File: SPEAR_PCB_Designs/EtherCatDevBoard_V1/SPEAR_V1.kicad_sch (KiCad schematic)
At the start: 25 parts, among them J1 Conn_ARM_SWD_TagConnect_TC2030, J2 USB_C_Receptacle_USB2.0_16P, SW1 SW_Push, SW2 SW_Push, U1 STM32F446RCTx, U2 USBLC6-2SC6, Y1 16MHz

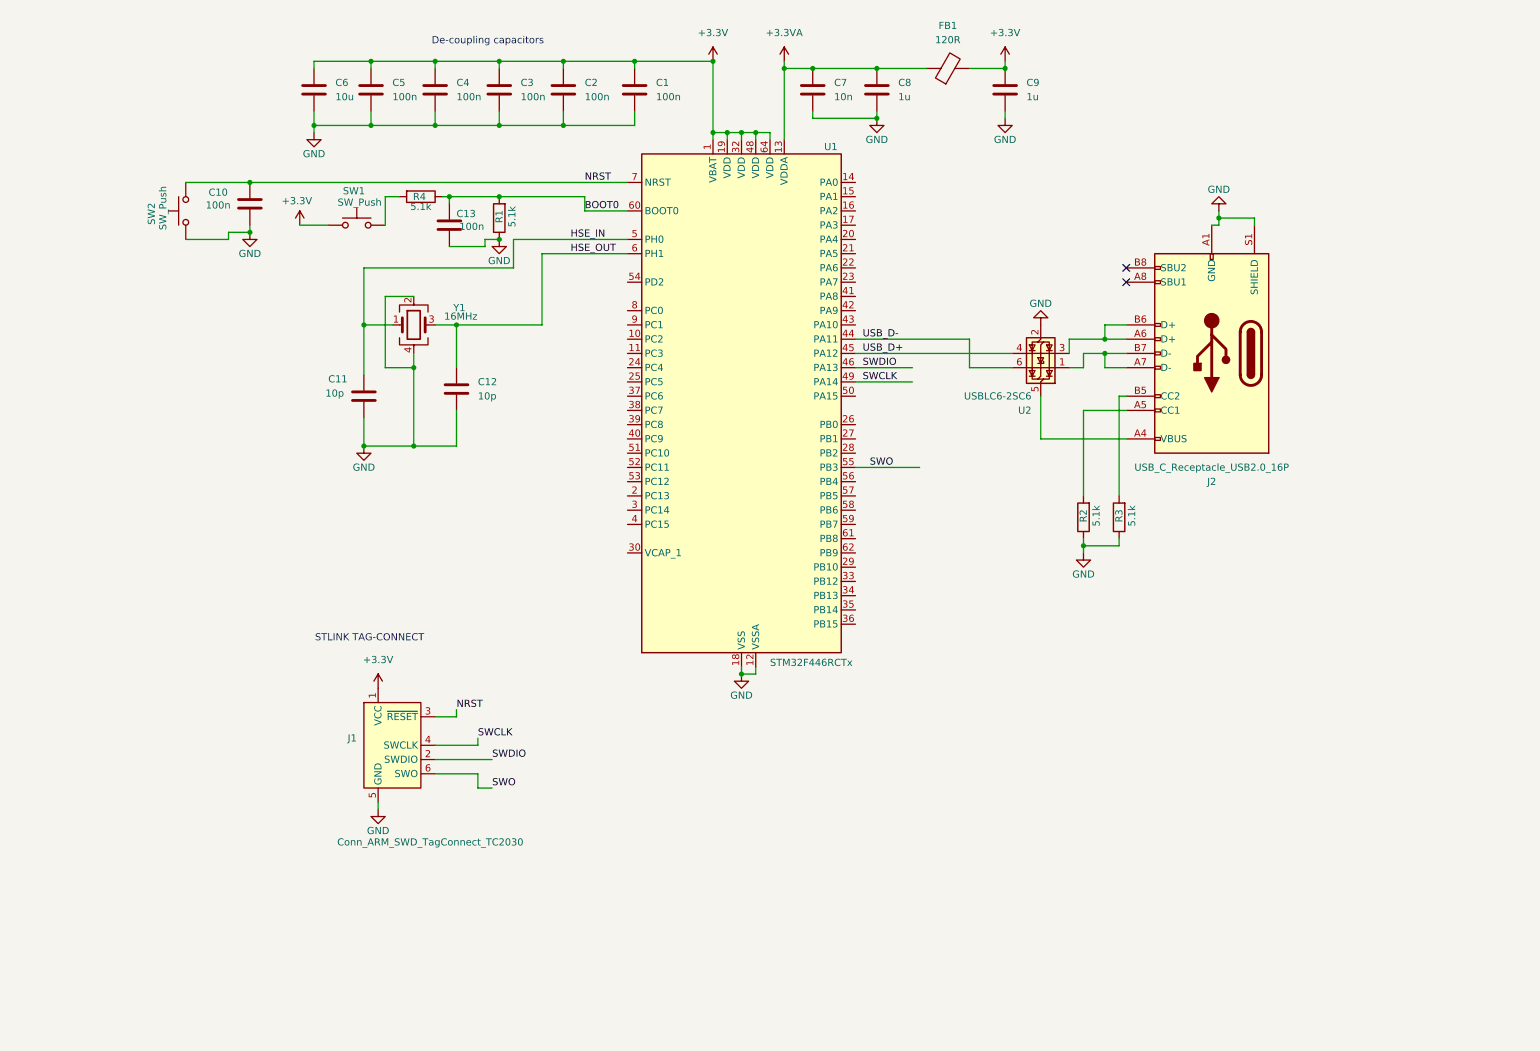
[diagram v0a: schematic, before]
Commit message: Update SPEAR_V1.kicad_sch
added communication protocols, esd protection for usb, voltage regulator
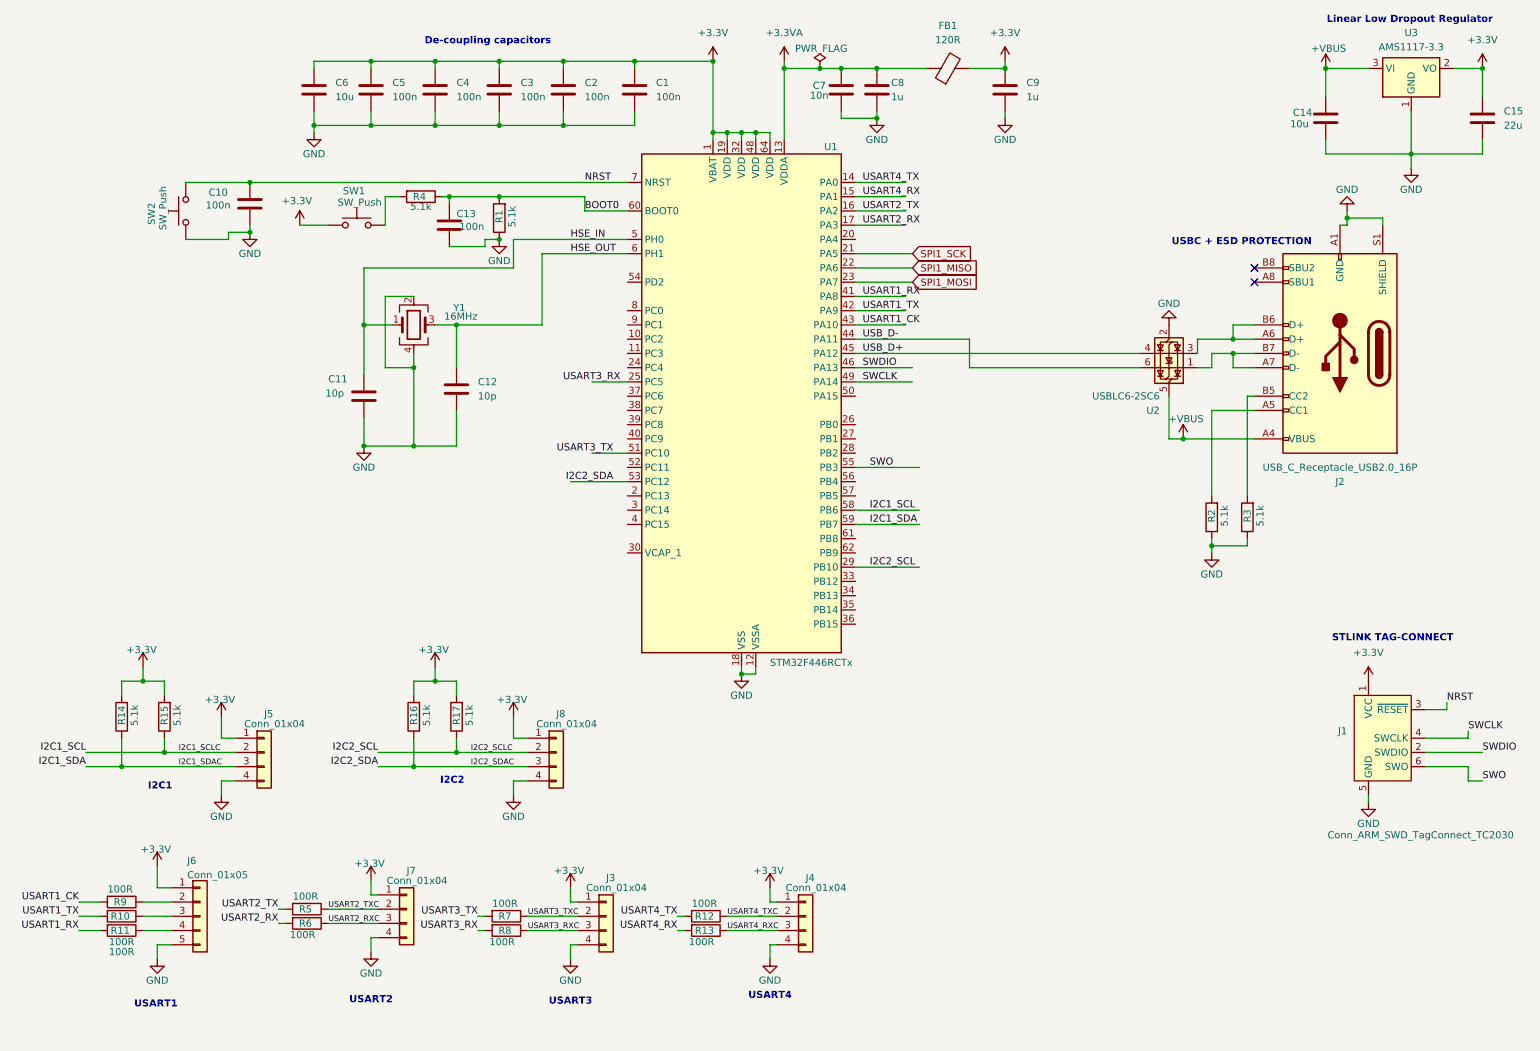
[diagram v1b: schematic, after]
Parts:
- added C14: 10u, symbol Device:C
- added C15: 22u, symbol Device:C
- added J3, J4, J5, J7, J8: Conn_01x04, symbol Connector_Generic:Conn_01x04
- added J6: Conn_01x05, symbol Connector_Generic:Conn_01x05
- added R10, R11, R12, R13, R5, R6, R7, R8, R9: 100R, symbol Device:R
- added R14, R15, R16, R17: 5.1k, symbol Device:R
- added U3: AMS1117-3.3, Package_TO_SOT_SMD:SOT-223-3_TabPin2, symbol Regulator_Linear:AMS1117-3.3
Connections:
- net +3.3V: now also C15.1, J3.1 (Pin_1), J4.1 (Pin_1), J5.1 (Pin_1), J6.1 (Pin_1), J7.1 (Pin_1), J8.1 (Pin_1), R14.2, R15.2, R16.2, R17.2, U3.2 (VO)
- net GND: now also C14.2, C15.2, J3.4 (Pin_4), J4.4 (Pin_4), J5.4 (Pin_4), J6.5 (Pin_5), J7.4 (Pin_4), J8.4 (Pin_4), U3.1 (GND)
- net USART4_TX: now reaches U1.14 (PA0)
- net USART4_TX: now also R12.2
- net USART4_RX: now reaches U1.15 (PA1)
- net USART4_RX: now also R13.2
- net USART2_TX: now reaches U1.16 (PA2)
- net USART2_TX: now also R5.2
- net USART2_RX: now reaches U1.17 (PA3)
- net USART2_RX: now also R6.2
- net SPI1_SCK: now reaches U1.21 (PA5)
- net SPI1_MISO: now reaches U1.22 (PA6)
- net SPI1_MOSI: now reaches U1.23 (PA7)
- net USART3_RX: now reaches U1.25 (PC5)
- net USART3_RX: now also R8.2
- net I2C2_SCL: now reaches U1.29 (PB10)
- net I2C2_SCL: now also J8.2 (Pin_2), R17.1
- net USART1_RX: now reaches U1.41 (PA8)
- net USART1_RX: now also R11.2
- net USART1_TX: now reaches U1.42 (PA9)
- net USART1_TX: now also R10.2
- net USART1_CK: now reaches U1.43 (PA10)
- net USART1_CK: now also R9.2
- net USART3_TX: now reaches U1.51 (PC10)
- net USART3_TX: now also R7.2
- net I2C2_SDA: now reaches U1.53 (PC12)
- net I2C2_SDA: now also J8.3 (Pin_3), R16.1
- net I2C1_SCL: now reaches U1.58 (PB6)
- net I2C1_SCL: now also J5.2 (Pin_2), R15.1
- net I2C1_SDA: now reaches U1.59 (PB7)
- net I2C1_SDA: now also J5.3 (Pin_3), R14.1
- net +VBUS: now reaches J2.A4 (VBUS), J2.A9 (VBUS), J2.B4 (VBUS), J2.B9 (VBUS), U2.5 (VBUS)
- net +VBUS: now also C14.1, U3.3 (VI)
- new net: J6.4 (Pin_4), R11.1
- new net: J6.3 (Pin_3), R10.1
- new net: J6.2 (Pin_2), R9.1
- new net USART2_RXC: J7.3 (Pin_3), R6.1
- new net USART2_TXC: J7.2 (Pin_2), R5.1
- new net USART3_RXC: J3.3 (Pin_3), R8.1
- new net USART3_TXC: J3.2 (Pin_2), R7.1
- new net USART4_RXC: J4.3 (Pin_3), R13.1
- new net USART4_TXC: J4.2 (Pin_2), R12.1
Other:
- note added: "I2C1"
- note added: "I2C2"
- note added: "Linear Low Dropout Regulator"
- note added: "USART1"
- note added: "USART2"
- note added: "USART3"
- note added: "USART4"
- note added: "USBC + ESD PROTECTION"
- moved on the sheet: C7, J1, J2, R2, R3, U2

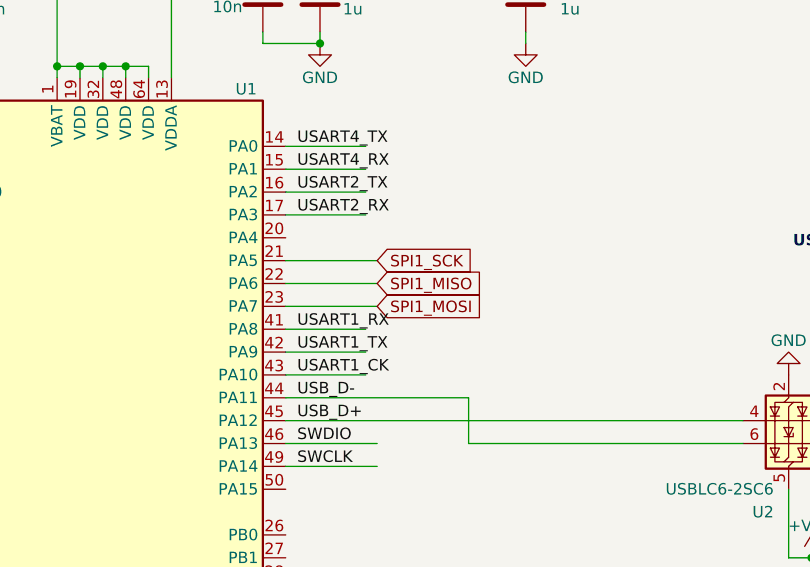
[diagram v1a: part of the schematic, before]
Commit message: Merged
merged LAN and EtherCAT
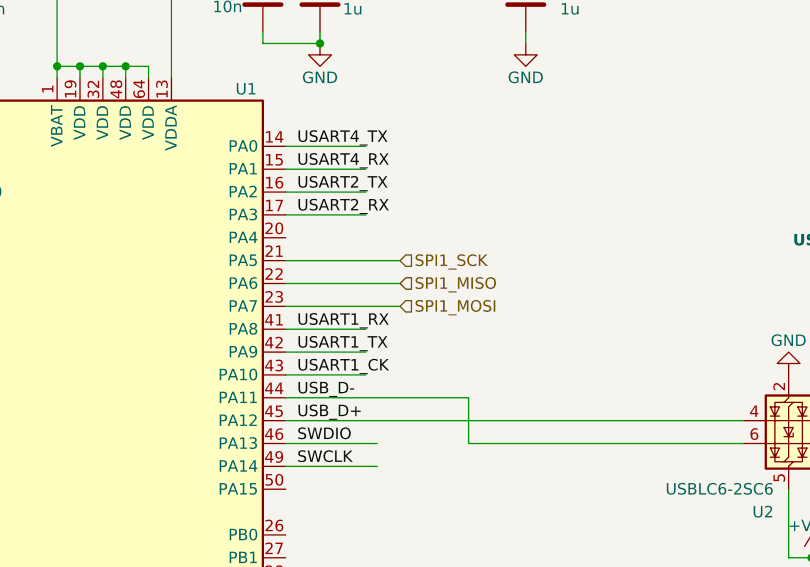
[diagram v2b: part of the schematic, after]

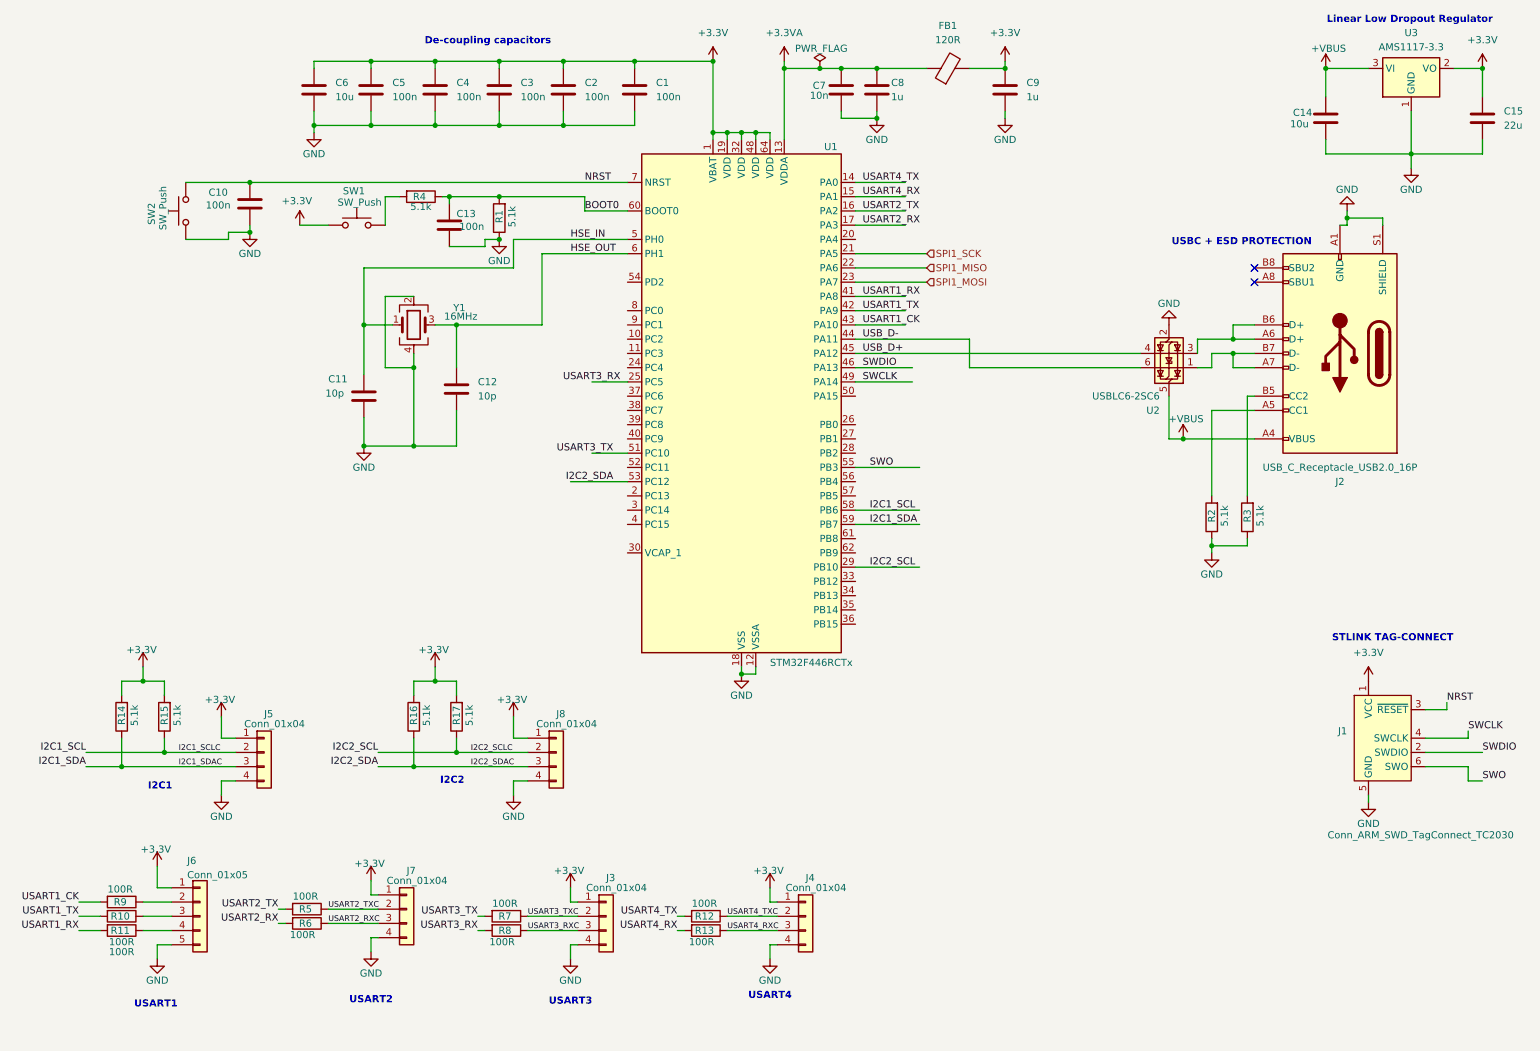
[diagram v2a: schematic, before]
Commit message: Header pins, st-link and vcap
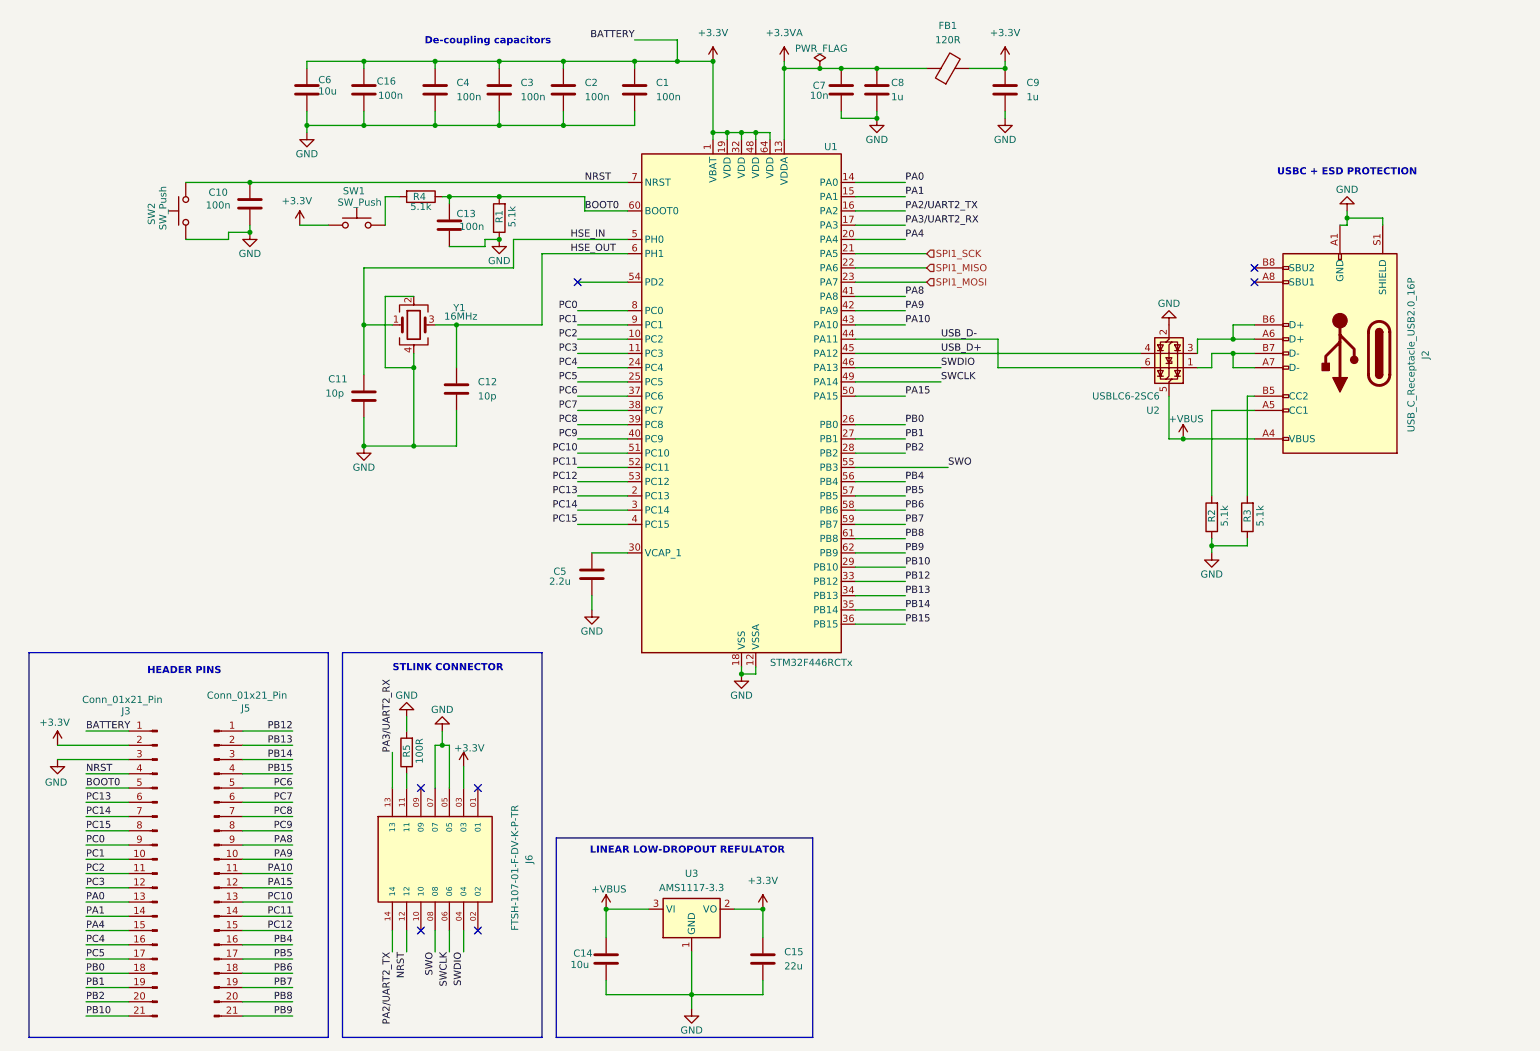
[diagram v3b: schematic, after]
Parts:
- removed J1: Conn_ARM_SWD_TagConnect_TC2030, Connector:Tag-Connect_TC2030-IDC-FP_2x03_P1.27mm_Vertical, symbol Connector:Conn_ARM_SWD_TagConnect_TC2030
- removed J3, J4, J5, J7, J8: Conn_01x04, symbol Connector_Generic:Conn_01x04
- removed J6: Conn_01x05, symbol Connector_Generic:Conn_01x05
- removed R10, R11, R12, R13, R6, R7, R8, R9: 100R, symbol Device:R
- removed R14, R15, R16, R17: 5.1k, symbol Device:R
- added C16: 100n, symbol Device:C
- added J3, J5: Conn_01x21_Pin, symbol Connector:Conn_01x21_Pin
- added J6: FTSH-107-01-F-DV-K-P-TR, FTSH-107-01-F-DV-K-P-TR:SAMTEC_FTSH-107-01-F-DV-K-P-TR, symbol FTSH-107-01-F-DV-K-P-TR:FTSH-107-01-F-DV-K-P-TR
- C5: value 100n -> 2.2u
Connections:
- net +3.3V: now also C16.1, J3.1 (Pin_1), J3.2 (Pin_2), J6.03; no longer C5.1
- net BOOT0: now also J3.5 (Pin_5)
- net GND: now also R5.2, C16.2, J3.3 (Pin_3), J6.05, J6.07
- net NRST: now also J3.4 (Pin_4), J6.12
- net SWCLK: now also J6.06
- net SWDIO: now also J6.04
- net SWO: now also J6.08
- net PC2: now reaches U1.10 (PC2)
- net PC2: now also J3.11 (Pin_11)
- net PC3: now reaches U1.11 (PC3)
- net PC3: now also J3.12 (Pin_12)
- net PC13: now reaches U1.2 (PC13)
- net PC13: now also J3.6 (Pin_6)
- net PA4: now reaches U1.20 (PA4)
- net PA4: now also J3.15 (Pin_15)
- net PC4: now reaches U1.24 (PC4)
- net PC4: now also J3.16 (Pin_16)
- net PB0: now reaches U1.26 (PB0)
- net PB0: now also J3.18 (Pin_18)
- net PB1: now reaches U1.27 (PB1)
- net PB1: now also J3.19 (Pin_19)
- net PB2: now reaches U1.28 (PB2)
- net PB2: now also J3.20 (Pin_20)
- net PC14: now reaches U1.3 (PC14)
- net PC14: now also J3.7 (Pin_7)
- net at U1.30 (VCAP_1): now also C5.1
- net PB12: now reaches U1.33 (PB12)
- net PB12: now also J5.1 (Pin_1)
- net PB13: now reaches U1.34 (PB13)
- net PB13: now also J5.2 (Pin_2)
- net PB14: now reaches U1.35 (PB14)
- net PB14: now also J5.3 (Pin_3)
- net PB15: now reaches U1.36 (PB15)
- net PB15: now also J5.4 (Pin_4)
- net PC6: now reaches U1.37 (PC6)
- net PC6: now also J5.5 (Pin_5)
- net PC7: now reaches U1.38 (PC7)
- net PC7: now also J5.6 (Pin_6)
- net PC8: now reaches U1.39 (PC8)
- net PC8: now also J5.7 (Pin_7)
- net PC15: now reaches U1.4 (PC15)
- net PC15: now also J3.8 (Pin_8)
- net PC9: now reaches U1.40 (PC9)
- net PC9: now also J5.8 (Pin_8)
- net PA15: now reaches U1.50 (PA15)
- net PA15: now also J5.12 (Pin_12)
- net PC11: now reaches U1.52 (PC11)
- net PC11: now also J5.14 (Pin_14)
- net PB4: now reaches U1.56 (PB4)
- net PB4: now also J5.16 (Pin_16)
- net PB5: now reaches U1.57 (PB5)
- net PB5: now also J5.17 (Pin_17)
- net PB8: now reaches U1.61 (PB8)
- net PB8: now also J5.20 (Pin_20)
- net PB9: now reaches U1.62 (PB9)
- net PB9: now also J5.21 (Pin_21)
- net PC0: now reaches U1.8 (PC0)
- net PC0: now also J3.9 (Pin_9)
- net PC1: now reaches U1.9 (PC1)
- net PC1: now also J3.10 (Pin_10)
- net I2C1_SCL renamed PB6
- net PB6: now also J5.18 (Pin_18)
- net I2C1_SDA renamed PB7
- net PB7: now also J5.19 (Pin_19)
- net I2C2_SCL renamed PB10
- net PB10: now also J3.21 (Pin_21)
- net I2C2_SDA renamed PC12
- net PC12: now also J5.15 (Pin_15)
- net USART1_CK renamed PA10
- net PA10: now also J5.11 (Pin_11)
- net USART1_RX renamed PA8
- net PA8: now also J5.9 (Pin_9)
- net USART1_TX renamed PA9
- net PA9: now also J5.10 (Pin_10)
- net USART2_RX renamed PA3/UART2_RX
- net PA3/UART2_RX: now also J6.13
- net USART2_TX renamed PA2/UART2_TX
- net PA2/UART2_TX: now also J6.14; no longer R5.2
- net USART2_TXC: no longer names the net of R5.1
- net USART2_TXC: now also J6.11
- net USART3_RX renamed PC5
- net PC5: now also J3.17 (Pin_17)
- net USART3_TX renamed PC10
- net PC10: now also J5.13 (Pin_13)
- net USART4_RX renamed PA1
- net PA1: now also J3.14 (Pin_14)
- net USART4_TX renamed PA0
- net PA0: now also J3.13 (Pin_13)
- no-connect marks 2 -> 7
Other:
- note added: "HEADER PINS"
- note added: "LINEAR LOW-DROPOUT REFULATOR"
- note added: "STLINK CONNECTOR"
- note removed: "I2C1"
- note removed: "I2C2"
- note removed: "Linear Low Dropout Regulator"
- note removed: "STLINK TAG-CONNECT"
- note removed: "USART1"
- note removed: "USART2"
- note removed: "USART3"
- note removed: "USART4"
- moved on the sheet: C14, C15, C6, U3
